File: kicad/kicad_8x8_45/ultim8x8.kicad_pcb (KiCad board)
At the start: 2 copper layers, 61 x 61 mm, 84 parts, among them P1 Input1, P10 DO_H, P11 5V, P12 GND, P2 Output1, P3 5V, P4 GND, P5 Input2, P6 Output2, P7 CI_A, P8 CO_H, P9 DI_A, U01 APA102, U02 APA102, U03 APA102, U04 APA102, U05 APA102, U06 APA102, U07 APA102, U08 APA102, U09 APA102, U10 APA102, U11 APA102, U12 APA102, U13 APA102, U14 APA102, U15 APA102, U16 APA102, U17 APA102, U18 APA102, U19 APA102, U20 APA102, U21 APA102, U22 APA102, U23 APA102, U24 APA102, U25 APA102, U26 APA102, U27 APA102, U28 APA102, U29 APA102, U30 APA102, U31 APA102, U32 APA102, U33 APA102, U34 APA102, U35 APA102, U36 APA102, U37 APA102, U38 APA102, U39 APA102, U40 APA102, U41 APA102, U42 APA102, U43 APA102, U44 APA102, U45 APA102, U46 APA102, U47 APA102, U48 APA102, U49 APA102, U50 APA102, U51 APA102, U52 APA102, U53 APA102, U54 APA102, U55 APA102, U56 APA102, U57 APA102, U58 APA102, U59 APA102, U60 APA102, U61 APA102, U62 APA102, U63 APA102, U64 APA102

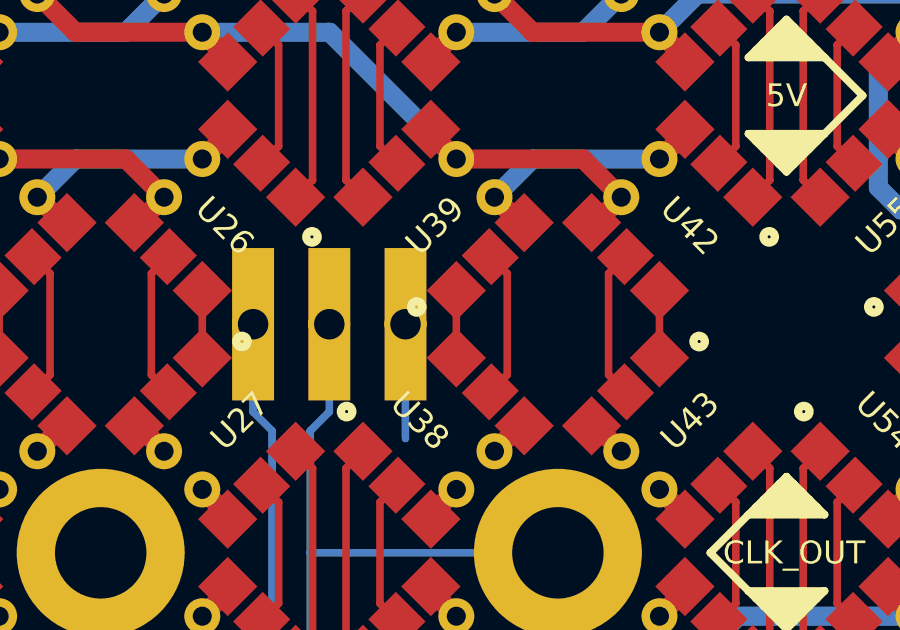
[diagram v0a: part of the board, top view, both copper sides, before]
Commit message: archived old kicad design in _old folder
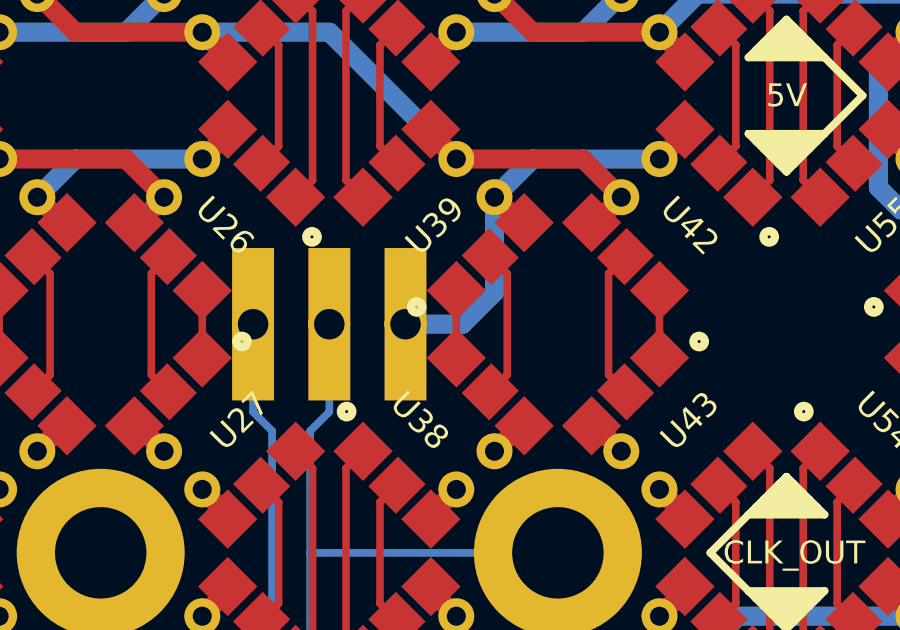
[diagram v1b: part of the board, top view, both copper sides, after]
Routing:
- net GND: track 292.9 -> 295.7 mm
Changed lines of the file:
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@@
     (links 420)
     (no_connects 0)
-    (area 29.082999 29.082999 90.297001 90.297001)
+    (area 18.138019 21.82368 99.616382 98.379281)
     (thickness 1.6002)
     (drawings 215)
-    (tracks 855)
+    (tracks 857)
     (zones 0)
     (modules 84)
@@
   (layers
     (0 Front signal hide)
-    (31 Back signal hide)
+    (31 Back signal)
     (32 B.Adhes user)
     (33 F.Adhes user)
     (34 B.Paste user)
     (35 F.Paste user)
-    (36 B.SilkS user)
-    (37 F.SilkS user)
+    (36 B.SilkS user hide)
+    (37 F.SilkS user hide)
     (38 B.Mask user)
     (39 F.Mask user)
-    (40 Dwgs.User user)
+    (40 Dwgs.User user hide)
     (41 Cmts.User user)
     (42 Eco1.User user)
@@
     (uvia_dia 0.508)
     (uvia_drill 0.127)
+    (diff_pair_gap 0.25)
+    (diff_pair_width 0.2)
     (add_net "Net-(U01-Pad5)")
     (add_net "Net-(U01-Pad6)")
@@
     (uvia_dia 0.508)
     (uvia_drill 0.127)
+    (diff_pair_gap 0.25)
+    (diff_pair_width 0.2)
     (add_net /Row_A/CI_A)
     (add_net /Row_A/CI_B)
@@
     (uvia_dia 0.508)
     (uvia_drill 0.127)
+    (diff_pair_gap 0.25)
+    (diff_pair_width 0.2)
   )
   (net_class 20mil ""
@@
     (uvia_dia 0.508)
     (uvia_drill 0.127)
+    (diff_pair_gap 0.25)
+    (diff_pair_width 0.2)
   )
   (net_class 25mil ""
@@
     (uvia_dia 0.508)
     (uvia_drill 0.127)
+    (diff_pair_gap 0.25)
+    (diff_pair_width 0.2)
     (add_net /Row_A/5V)
     (add_net GND)
@@
   (segment (start 57.785 48.006) (end 57.15 47.371) (width 0.254) (layer Back) (net 2))
   (segment (start 57.15 47.371) (end 57.15 44.45) (width 0.254) (layer Back) (net 2) (status 20))
+  (segment (start 65.197056 43.387944) (end 64.135 44.45) (width 0.635) (layer Back) (net 3))
+  (segment (start 64.135 44.45) (end 62.23 44.45) (width 0.635) (layer Back) (net 3))
+  (segment (start 65.197056 40.215736) (end 65.197056 43.387944) (width 0.635) (layer Back) (net 3))
   (segment (start 74.93 57.15) (end 72.136 57.15) (width 0.635) (layer Back) (net 3) (status 10))
   (segment (start 67.52632 57.785) (end 65.197056 55.455736) (width 0.635) (layer Back) (net 3) (status 20))
@@
   (segment (start 44.45 57.15) (end 48.262792 57.15) (width 0.635) (layer Back) (net 3) (status 10))
   (segment (start 48.262792 57.15) (end 49.957056 55.455736) (width 0.635) (layer Back) (net 3) (status 20))
-  (segment (start 62.23 48.26) (end 62.23 44.45) (width 0.254) (layer Back) (net 3) (status 20))
   (segment (start 55.455736 84.662944) (end 51.229848 84.662944) (width 0.635) (layer Back) (net 3) (status 10))
   (segment (start 51.229848 84.662944) (end 49.957056 85.935736) (width 0.635) (layer Back) (net 3) (status 20))

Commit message: board outline changed. upgraded 3 pin headers to 4 pins
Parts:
- P1, P2, P5, P6: footprint ultim8x8_libs:header_3pos_th_male -> ultim8x8_libs:header_2x2pos_th_male
- moved L2 0.63 mm to (59.7, 33.9)
- turned P1 to 180 degrees
- turned P2 to 90 degrees
- turned P5 to 270 degrees
- turned P6 to 180 degrees
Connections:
- net /Row_A/CI_B renamed /CI_B
- net /Row_A/DI_B renamed /DI_B
- net /Row_B/CI_C renamed /CI_C
- net /Row_B/DI_C renamed /DI_C
- net /Row_C/CI_D renamed /CI_D
- net /Row_C/DI_D renamed /DI_D
- net /Row_D/CI_E renamed /CI_E
- net /Row_D/DI_E renamed /DI_E
- net /Row_E/CI_F renamed /CI_F
- net /Row_E/DI_F renamed /DI_F
- net /Row_F/CI_G renamed /CI_G
- net /Row_F/DI_G renamed /DI_G
- net /Row_G/CI_H renamed /CI_H
- net /Row_G/DI_H renamed /DI_H
- net /Row_H/DO_H renamed /DO_H
- C1 pad 2: /Row_A/5V -> /5V
- C2 pad 1: /Row_A/5V -> /5V
- C3 pad 2: /Row_A/5V -> /5V
- C4 pad 1: /Row_A/5V -> /5V
- P1 pad 1: /Row_A/DI_A -> /DI_A
- P1 pad 2: /Row_A/CI_A -> /CI_A
- P11 pad 1: /Row_A/5V -> /5V
- P2 pad 2: /Row_H/CO_H -> /CO_H
- P3 pad 1: /Row_A/5V -> /5V
- P5 pad 1: GND -> /CI_A
- P5 pad 2: /Row_A/CI_A -> /DI_A
- P5 pad 3: /Row_A/DI_A -> /5V
- P6 pad 2: /Row_H/CO_H -> /5V
- P7 pad 1: /Row_A/CI_A -> /CI_A
- P8 pad 1: /Row_H/CO_H -> /CO_H
- P9 pad 1: /Row_A/DI_A -> /DI_A
- U01 pad 1: /Row_A/DI_A -> /DI_A
- U01 pad 2: /Row_A/CI_A -> /CI_A
- U01 pad 4: /Row_A/5V -> /5V
- U02 pad 4: /Row_A/5V -> /5V
- U03 pad 4: /Row_A/5V -> /5V
- U04 pad 4: /Row_A/5V -> /5V
- U05 pad 4: /Row_A/5V -> /5V
- U06 pad 4: /Row_A/5V -> /5V
- U07 pad 4: /Row_A/5V -> /5V
- U08 pad 4: /Row_A/5V -> /5V
- U09 pad 4: /Row_A/5V -> /5V
- U10 pad 4: /Row_A/5V -> /5V
- U11 pad 4: /Row_A/5V -> /5V
- U12 pad 4: /Row_A/5V -> /5V
- U13 pad 4: /Row_A/5V -> /5V
- U14 pad 4: /Row_A/5V -> /5V
- U15 pad 4: /Row_A/5V -> /5V
- U16 pad 4: /Row_A/5V -> /5V
- U17 pad 4: /Row_A/5V -> /5V
- U18 pad 4: /Row_A/5V -> /5V
- U19 pad 4: /Row_A/5V -> /5V
- U20 pad 4: /Row_A/5V -> /5V
- U21 pad 4: /Row_A/5V -> /5V
- U22 pad 4: /Row_A/5V -> /5V
- U23 pad 4: /Row_A/5V -> /5V
- U24 pad 4: /Row_A/5V -> /5V
- U25 pad 4: /Row_A/5V -> /5V
- U26 pad 4: /Row_A/5V -> /5V
- U27 pad 4: /Row_A/5V -> /5V
- U28 pad 4: /Row_A/5V -> /5V
- U29 pad 4: /Row_A/5V -> /5V
- U30 pad 4: /Row_A/5V -> /5V
- U31 pad 4: /Row_A/5V -> /5V
- U32 pad 4: /Row_A/5V -> /5V
- U33 pad 4: /Row_A/5V -> /5V
- U34 pad 4: /Row_A/5V -> /5V
- U35 pad 4: /Row_A/5V -> /5V
- U36 pad 4: /Row_A/5V -> /5V
- U37 pad 4: /Row_A/5V -> /5V
- U38 pad 4: /Row_A/5V -> /5V
- U39 pad 4: /Row_A/5V -> /5V
- U40 pad 4: /Row_A/5V -> /5V
- U41 pad 4: /Row_A/5V -> /5V
- U42 pad 4: /Row_A/5V -> /5V
- U43 pad 4: /Row_A/5V -> /5V
- U44 pad 4: /Row_A/5V -> /5V
- U45 pad 4: /Row_A/5V -> /5V
- U46 pad 4: /Row_A/5V -> /5V
- U47 pad 4: /Row_A/5V -> /5V
- U48 pad 4: /Row_A/5V -> /5V
- U49 pad 4: /Row_A/5V -> /5V
- U50 pad 4: /Row_A/5V -> /5V
- U51 pad 4: /Row_A/5V -> /5V
- U52 pad 4: /Row_A/5V -> /5V
- U53 pad 4: /Row_A/5V -> /5V
- U54 pad 4: /Row_A/5V -> /5V
- U55 pad 4: /Row_A/5V -> /5V
- U56 pad 4: /Row_A/5V -> /5V
- U57 pad 4: /Row_A/5V -> /5V
- U58 pad 4: /Row_A/5V -> /5V
- U59 pad 4: /Row_A/5V -> /5V
- U60 pad 4: /Row_A/5V -> /5V
- U61 pad 4: /Row_A/5V -> /5V
- U62 pad 4: /Row_A/5V -> /5V
- U63 pad 4: /Row_A/5V -> /5V
- U64 pad 4: /Row_A/5V -> /5V
- U64 pad 5: /Row_H/CO_H -> /CO_H
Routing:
- net /5V: track 0.00 -> 372.3 mm
- net /Row_A/5V: track 350.5 -> 0.00 mm
- net /Row_H/CO_H: track 85.0 -> 0.00 mm, vias 1 -> 0
- net /CO_H: track 0.00 -> 81.4 mm, vias 0 -> 1
- net /CI_A: track 0.00 -> 79.0 mm, vias 0 -> 1
- net /Row_A/CI_A: track 77.9 -> 0.00 mm, vias 1 -> 0
- net /DI_A: track 0.00 -> 77.4 mm, vias 0 -> 1
- net /Row_A/DI_A: track 75.0 -> 0.00 mm, vias 1 -> 0
- net GND: track 295.7 -> 278.9 mm
- net /DO_H: track 80.1 -> 76.8 mm
- net /DI_E: track 8.47 -> 9.33 mm
- added copper zone on F.Cu, net /5V
- removed copper zone on F.Cu, net /Row_A/5V
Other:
- outline, holes or cut-outs redrawn
- board text added: "+5V GND"
- board text added: "CI_A DI_A"
- board text added: "CO_H DO_H"
- board text added: "DI_A CI_A"
- board text added: "DO_H CO_H"
- board text added: "GND +5V"
- board text removed: "DI_A CI_A GND"
- board text removed: "DO_H CO_H GND"
- board text removed: "GND CI_A DI_A"
- board text removed: "GND CO_H DO_H"

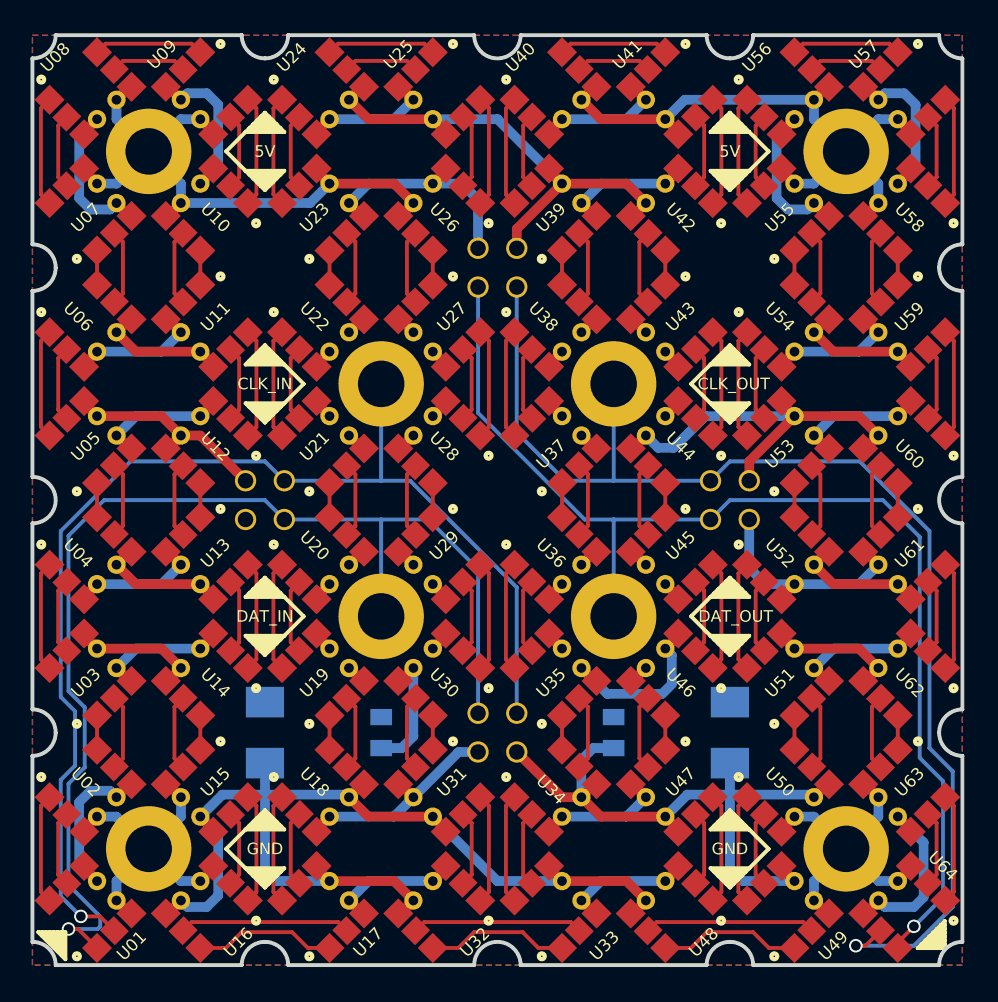
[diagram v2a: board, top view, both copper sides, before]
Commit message: rotated 4 pin headers by 45 deg
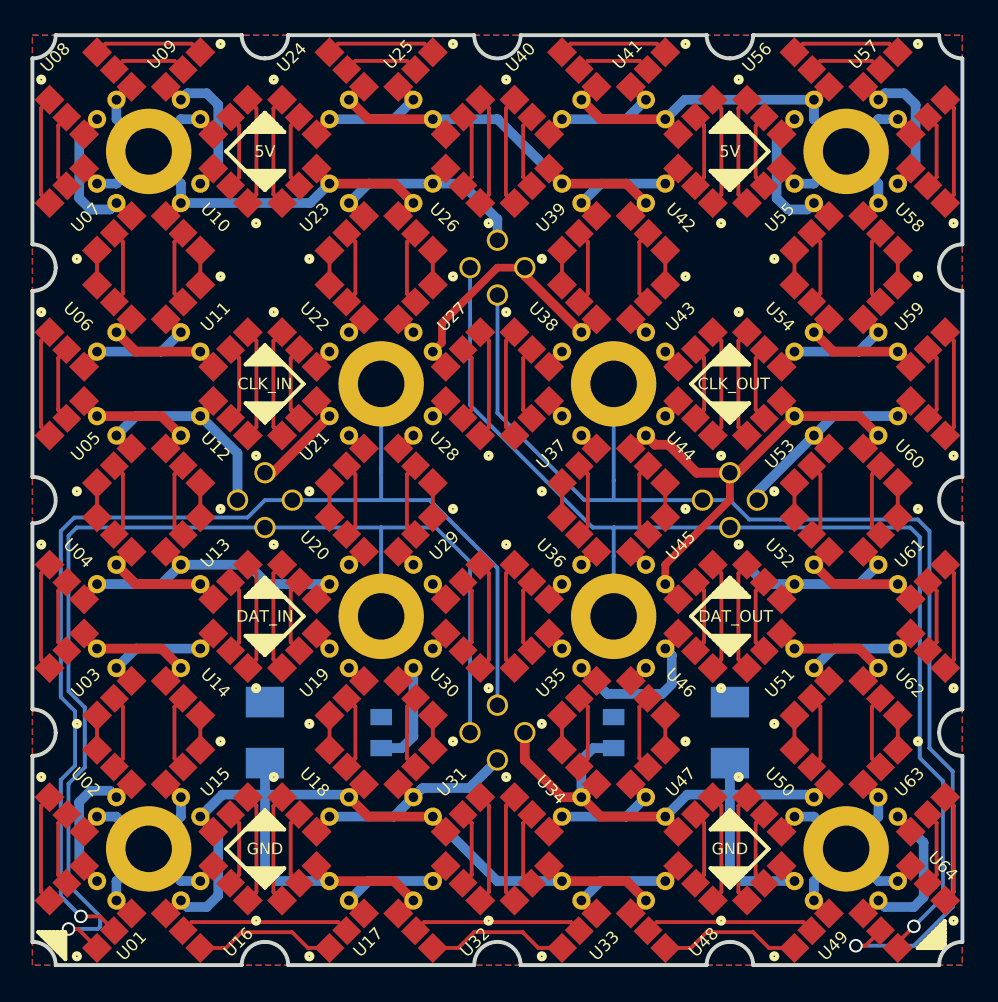
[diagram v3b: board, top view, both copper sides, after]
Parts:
- turned P1 to 135 degrees
- turned P2 to 45 degrees
- turned P5 to 315 degrees
- turned P6 to 225 degrees
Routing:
- net GND: track 278.9 -> 299.3 mm
- net /5V: track 372.3 -> 388.0 mm
- net /CI_A: track 79.0 -> 77.4 mm
- net /DI_A: track 77.4 -> 76.4 mm
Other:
- board text removed: "DI_A CI_A"
